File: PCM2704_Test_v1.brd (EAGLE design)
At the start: 54.1 x 35.4 mm, 50 parts, among them IC1 REG1117, IC2 REG1117, X1 USB-MB-S

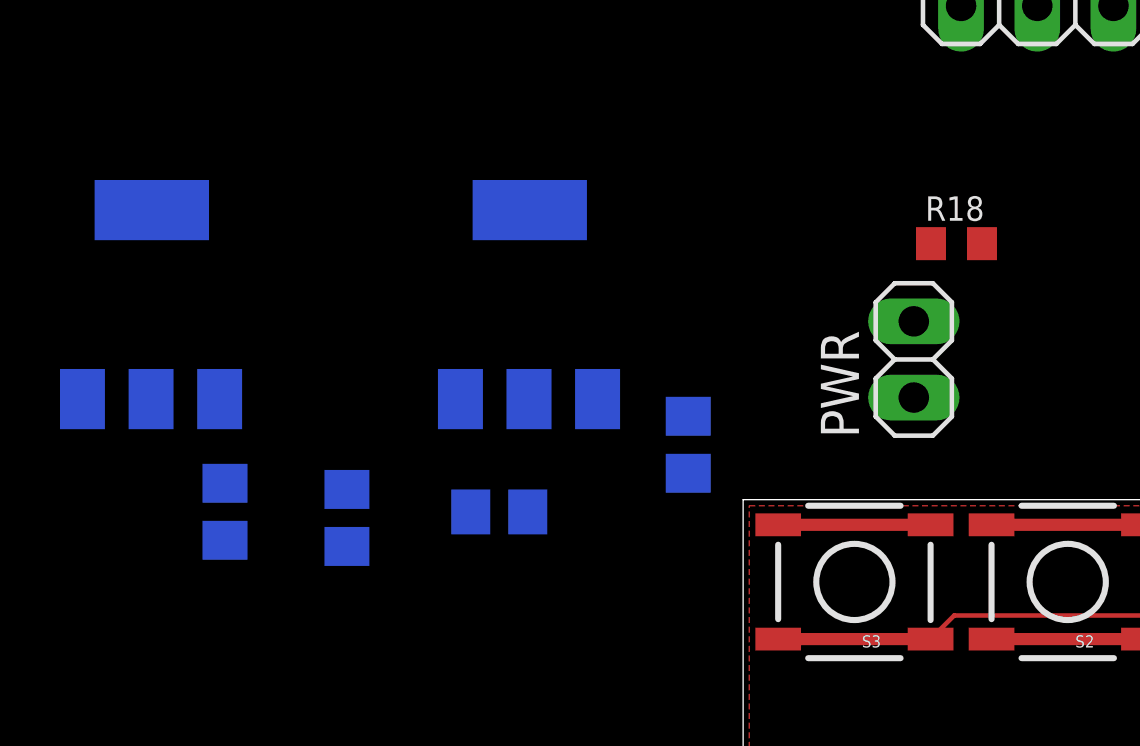
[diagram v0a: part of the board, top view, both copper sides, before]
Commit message: Removed Voltage Regulators
For VBUS operation, no voltage regulators are required. I removed both
of them from the board along with all supporting components such as
filter caps, etc.
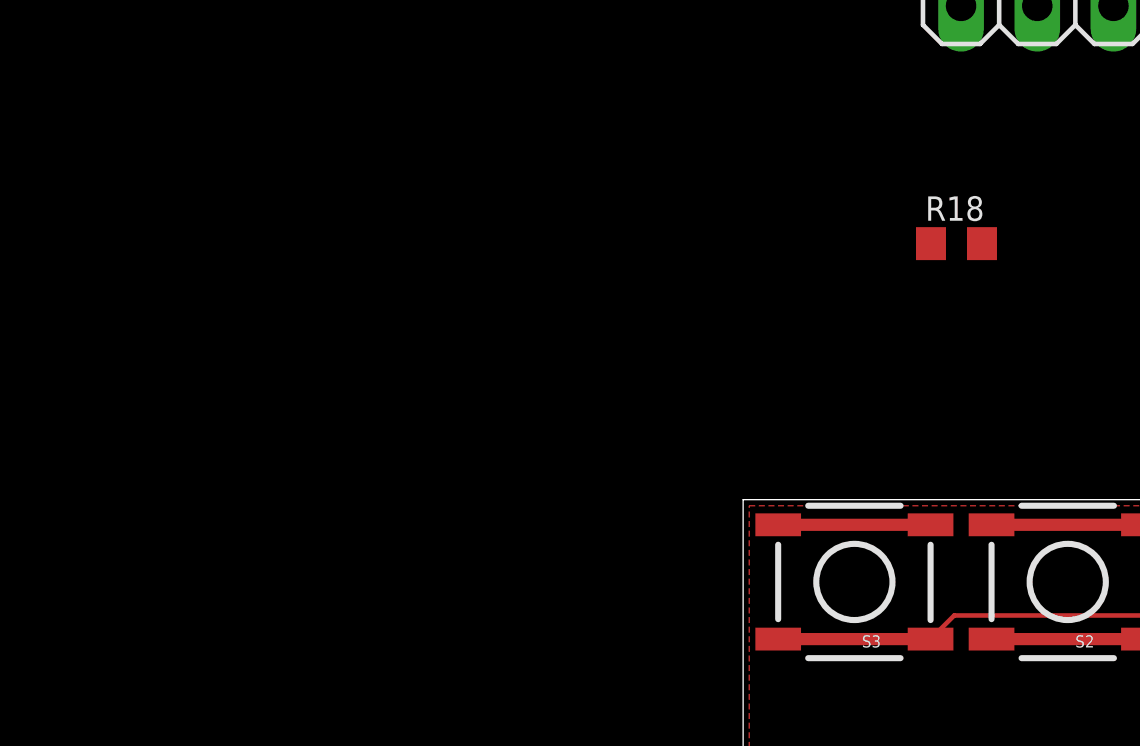
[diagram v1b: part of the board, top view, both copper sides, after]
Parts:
- removed C13, C14, C15, C16: 1u, rcl:C0805
- removed IC1, IC2: REG1117, burr-brown-3:SOT223
- removed PWR: (no value), pinhead:1X02
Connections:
- removed net VIN: C13.1, IC1.3, PWR.1
- net 5V: no longer C14.1, C15.1, IC1.2, IC2.3
- net GND: no longer C13.2, C14.2, C15.2, C16.2, IC1.1, IC2.1, PWR.2
- net VDD: no longer C16.1, IC2.2
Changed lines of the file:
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@@
 </element>
 <element name="U$2" library="SparkFun-Connectors" package="AUDIO-JACK-TRRS-SMD" value="AUDIO-JACK3" x="61.1632" y="44.9072" rot="R180"/>
-<element name="C13" library="rcl" package="C0805" value="1u" x="-10.7696" y="32.7152" rot="MR270"/>
-<element name="C14" library="rcl" package="C0805" value="1u" x="-14.8336" y="32.9184" rot="MR90"/>
-<element name="IC1" library="burr-brown-3" package="SOT223" value="REG1117" x="-4.6736" y="39.8272" rot="MR0"/>
-<element name="IC2" library="burr-brown-3" package="SOT223" value="REG1117" x="-17.272" y="39.8272" rot="MR0"/>
-<element name="C15" library="rcl" package="C0805" value="1u" x="-5.6896" y="32.9184" rot="MR180"/>
-<element name="C16" library="rcl" package="C0805" value="1u" x="0.6096" y="35.1536" rot="MR90"/>
-<element name="PWR" library="pinhead" package="1X02" value="" x="8.128" y="37.9984" rot="R90"/>
 <element name="L1" library="rcl" package="L3225M" value="" x="13.0048" y="8.5344" rot="R90"/>
 <element name="JPBUS" library="pinhead" package="1X02" value="" x="7.112" y="13.208" rot="R90"/>
@@
 <contactref element="R6" pad="1"/>
 <contactref element="U$2" pad="RING2"/>
-<contactref element="C13" pad="2"/>
-<contactref element="C14" pad="2"/>
-<contactref element="IC1" pad="1"/>
-<contactref element="IC2" pad="1"/>
-<contactref element="IC1" pad="1"/>
-<contactref element="C15" pad="2"/>
-<contactref element="IC2" pad="1"/>
-<contactref element="C16" pad="2"/>
-<contactref element="PWR" pad="2"/>
 <contactref element="R2" pad="2"/>
 <contactref element="U$1" pad="6"/>
@@
 <wire x1="57.9632" y1="41.6572" x2="50.5968" y2="37.3024" width="0" layer="19" extent="1-1"/>
 <wire x1="36.942" y1="23.368" x2="50.5968" y2="37.3024" width="0" layer="19" extent="1-1"/>
-<wire x1="8.128" y1="39.2684" x2="15.8242" y2="20.701" width="0" layer="19" extent="1-1"/>
-<wire x1="0.6096" y1="36.1036" x2="8.128" y2="39.2684" width="0" layer="19" extent="16-16"/>
-<wire x1="-2.413" y1="36.6776" x2="0.6096" y2="36.1036" width="0" layer="19" extent="16-16"/>
-<wire x1="-4.7396" y1="32.9184" x2="-2.413" y2="36.6776" width="0" layer="19" extent="16-16"/>
-<wire x1="-10.7696" y1="31.7652" x2="-4.7396" y2="32.9184" width="0" layer="19" extent="16-16"/>
-<wire x1="-14.8336" y1="33.8684" x2="-10.7696" y2="31.7652" width="0" layer="19" extent="16-16"/>
-<wire x1="-15.0114" y1="36.6776" x2="-14.8336" y2="33.8684" width="0" layer="19" extent="16-16"/>
-<wire x1="22.4028" y1="49.784" x2="8.128" y2="39.2684" width="0" layer="19" extent="1-1"/>
+<wire x1="34.9498" y1="20.56" x2="36.2498" y2="20.56" width="0" layer="19" extent="1-1"/>
+<wire x1="35.56" y1="24.6276" x2="36.942" y2="23.368" width="0" layer="19" extent="1-1"/>
+<wire x1="34.3408" y1="24.6276" x2="35.56" y2="24.6276" width="0" layer="19" extent="1-1"/>
+<wire x1="36.2498" y1="12.46" x2="36.2498" y2="20.56" width="0" layer="19" extent="1-1"/>
+<wire x1="35.5998" y1="12.46" x2="36.2498" y2="12.46" width="0" layer="19" extent="1-1"/>
+<wire x1="32.3498" y1="12.46" x2="35.5998" y2="12.46" width="0" layer="19" extent="1-1"/>
+<wire x1="28.4108" y1="10.16" x2="31.4556" y2="10.1092" width="0" layer="19" extent="1-1"/>
+<wire x1="22.3116" y1="9.5504" x2="28.4108" y2="10.16" width="0" layer="19" extent="1-1"/>
+<wire x1="18.3642" y1="15.4686" x2="22.3116" y2="9.5504" width="0" layer="19" extent="1-1"/>
+<wire x1="17.0942" y1="15.4686" x2="18.3642" y2="15.4686" width="0" layer="19" extent="1-1"/>
+<wire x1="15.8242" y1="15.4686" x2="17.0942" y2="15.4686" width="0" layer="19" extent="1-1"/>
+<wire x1="14.5542" y1="15.4686" x2="15.8242" y2="15.4686" width="0" layer="19" extent="1-1"/>
+<wire x1="10.3228" y1="14.4272" x2="14.5542" y2="15.4686" width="0" layer="19" extent="1-1"/>
+<wire x1="10.1228" y1="13.0048" x2="10.3228" y2="14.4272" width="0" layer="19" extent="1-1"/>
+<wire x1="10.1228" y1="11.5824" x2="10.1228" y2="13.0048" width="0" layer="19" extent="1-1"/>
+<wire x1="15.8242" y1="20.701" x2="15.8242" y2="15.4686" width="0" layer="19" extent="1-1"/>
+<wire x1="22.1084" y1="22.9616" x2="15.8242" y2="20.701" width="0" layer="19" extent="1-1"/>
+<wire x1="9.6628" y1="2.3116" x2="10.1228" y2="11.5824" width="0" layer="19" extent="1-1"/>
+<wire x1="22.4028" y1="49.784" x2="42.738" y2="45.1104" width="0" layer="19" extent="1-1"/>
 </signal>
 <signal name="VDD">
-<contactref element="IC2" pad="2"/>
-<contactref element="C16" pad="1"/>
 <contactref element="U$1" pad="7"/>
 <contactref element="C3" pad="2"/>
@@
 <wire x1="14.5542" y1="20.701" x2="20.1168" y2="17.2348" width="0" layer="19" extent="1-1"/>
 <wire x1="11.85" y1="1.9304" x2="20.1168" y2="17.2348" width="0" layer="19" extent="1-1"/>
-<wire x1="0.6096" y1="34.2036" x2="14.5542" y2="20.701" width="0" layer="19" extent="1-16"/>
-<wire x1="-17.2974" y1="36.6776" x2="0.6096" y2="34.2036" width="0" layer="19" extent="16-16"/>
 </signal>
 <signal name="VBUS_RAW">
@@
 <wire x1="29.7498" y1="20.56" x2="23.5712" y2="39.9932" width="0" layer="19" extent="1-1"/>
 </signal>
-<signal name="VIN">
-<contactref element="C13" pad="1"/>
-<contactref element="IC1" pad="3"/>
-<contactref element="PWR" pad="1"/>
-<wire x1="-6.985" y1="36.6776" x2="8.128" y2="36.7284" width="0" layer="19" extent="16-16"/>
-<wire x1="-10.7696" y1="33.6652" x2="-6.985" y2="36.6776" width="0" layer="19" extent="16-16"/>
-</signal>
 <signal name="5V">
-<contactref element="C14" pad="1"/>
-<contactref element="IC1" pad="2"/>
-<contactref element="IC2" pad="3"/>
-<contactref element="C15" pad="1"/>
 <contactref element="JPBUS" pad="2"/>
-<wire x1="-6.6396" y1="32.9184" x2="-4.699" y2="36.6776" width="0" layer="19" extent="16-16"/>
-<wire x1="-14.8336" y1="31.9684" x2="-6.6396" y2="32.9184" width="0" layer="19" extent="16-16"/>
-<wire x1="-19.5834" y1="36.6776" x2="-14.8336" y2="31.9684" width="0" layer="19" extent="16-16"/>
-<wire x1="7.112" y1="14.478" x2="-6.6396" y2="32.9184" width="0" layer="19" extent="16-16"/>
 </signal>
 <signal name="N$5">

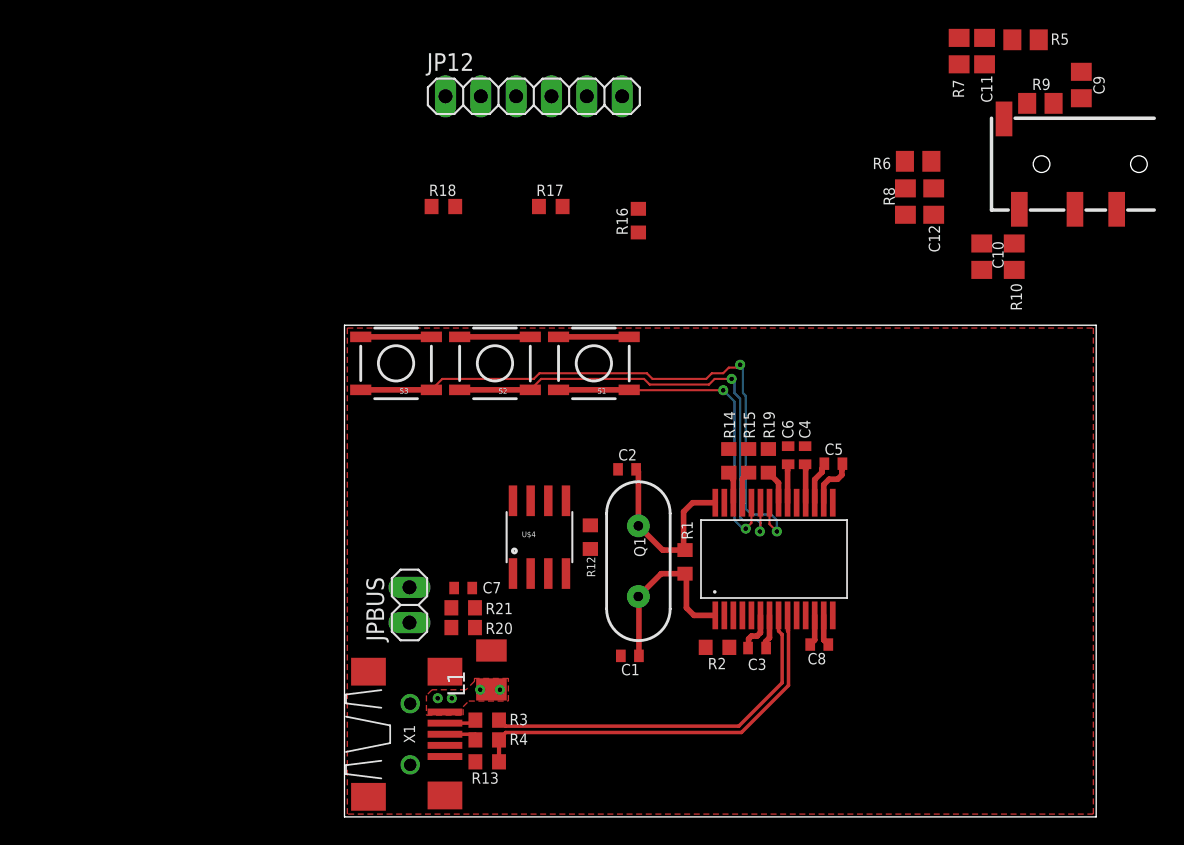
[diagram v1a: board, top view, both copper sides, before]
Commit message: Removed unnecessary components
Removed:
-  Function Buttons
-  Resistors associated with the buttons

Moved some components around to make better use of the space on the
board. Decreased the board length and width. Routed the EEPROM traces
and added a bypass capacitor footprint to the power pin of the EEPROM.

Ripped up some traces and instead used polygon pours to route the
signals to make them lower impedance traces. This includes the traces
routed to the headphone jack and the USB VBUS pin.
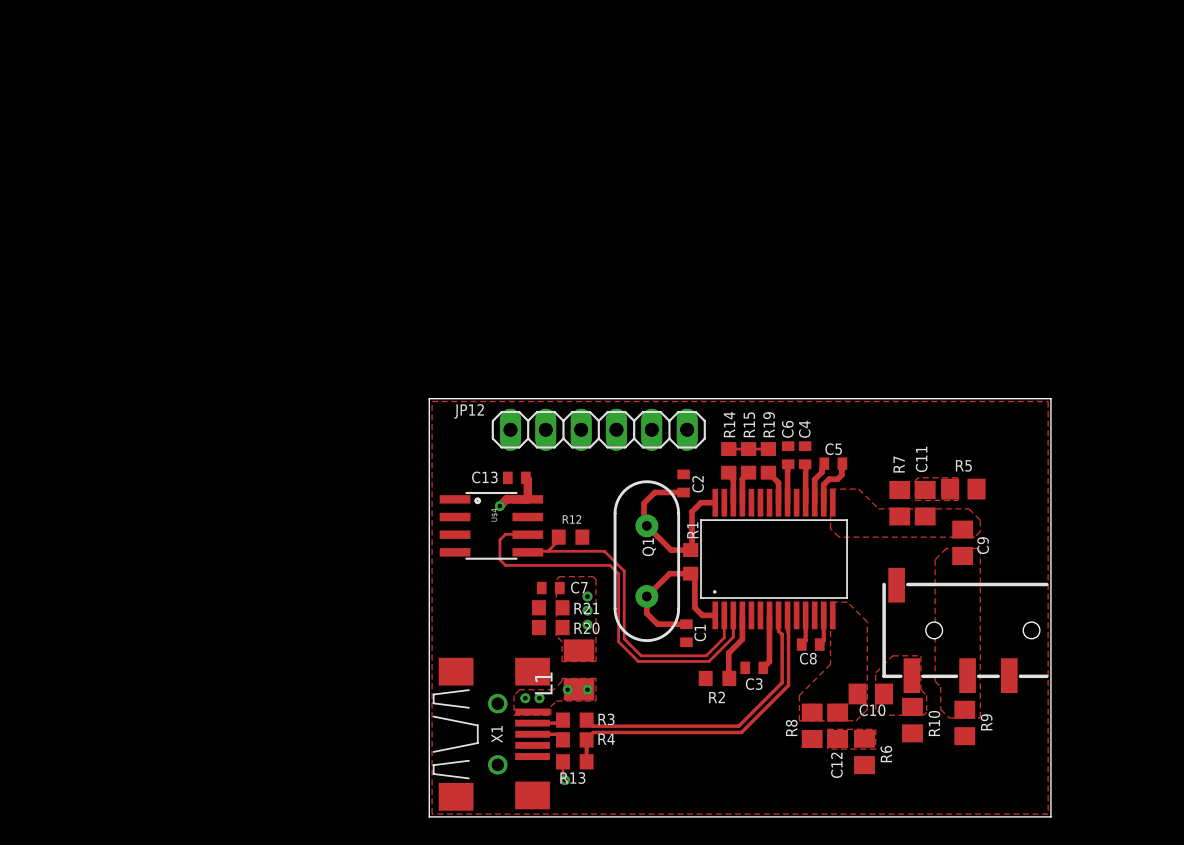
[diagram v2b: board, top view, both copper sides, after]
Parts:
- removed JPBUS: (no value), pinhead:1X02
- removed R16, R17, R18: 1k5, rcl:R0603
- removed S1, S2, S3: (no value), SparkFun:TACTILE_SWITCH_SMD
- added C13: 1u, rcl:C0402
- moved R9 44.9 mm to (47.0, 4.72), turned to 90 degrees
- moved R6 42.6 mm to (39.8, 2.64), turned to 90 degrees
- moved C12 38.3 mm to (37.9, 4.52), turned to 270 degrees
- moved R8 38.3 mm to (36.1, 4.52), turned to 90 degrees
- moved U$2 34.4 mm to (53.4, 11.4)
- moved R10 34.1 mm to (43.3, 4.93)
- moved C9 34.0 mm to (46.9, 17.7)
- moved C11 32.8 mm to (44.2, 20.5)
- moved R7 32.8 mm to (42.4, 20.5)
- moved R5 32.6 mm to (46.9, 21.5)
- moved C10 32.4 mm to (40.3, 6.81), turned to 0 degrees
- moved JP12 24.4 mm to (20.7, 25.8)
- moved X1 6.30 mm to (13.5, 3.91)
- moved C7 6.30 mm to (17.3, 14.4)
- moved L1 6.30 mm to (19.3, 8.53)
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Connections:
- removed net 5V: JPBUS.2
- removed net N$10: R17.1, S2.3, S2.4
- removed net N$11: R18.1, S3.3, S3.4
- removed net N$22: JP12.4, S3.1, S3.2, U$1.22
- removed net N$23: JP12.3, S2.1, S2.2, U$1.23
- removed net N$24: JP12.2, S1.1, S1.2, U$1.24
- removed net N$8: R16.1, S1.3, S1.4
- net GND: now also C13.2
- net SSPND: no longer R16.2, R17.2, R18.2
- net VBUS_RAW: no longer JPBUS.1
- net VDD: now also C13.1
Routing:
- net N$22: track 44.6 -> 0.00 mm, vias 2 -> 0
- net N$23: track 34.8 -> 0.00 mm, vias 2 -> 0
- net N$17: track 0.00 -> 28.6 mm
- net N$24: track 24.6 -> 0.00 mm, vias 2 -> 0
- net N$16: track 0.00 -> 23.6 mm
- net VDD: track 11.2 -> 20.7 mm, vias 0 -> 2
- net D_P: track 29.2 -> 22.9 mm
- net D_N: track 26.8 -> 20.5 mm
- net N$11: track 5.08 -> 0.00 mm
- net N$10: track 5.08 -> 0.00 mm
- net N$8: track 5.08 -> 0.00 mm
- net N$5: track 0.00 -> 4.95 mm
- net GND: track 8.25 -> 5.28 mm
- net N$1: track 13.1 -> 12.5 mm
- net VBUS: vias 0 -> 3
- added copper zone on layer 1, net HP_OUT_L
- added copper zone on layer 1, net HP_OUT_R
- added copper zone on layer 1, net N$19
- added copper zone on layer 1, net N$20
- added copper zone on layer 1, net VBUS
- added copper zone on layer 1, net VOUTL
- added copper zone on layer 1, net VOUTR
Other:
- board size 54.1 x 35.4 mm -> 44.7 x 30.1 mm
